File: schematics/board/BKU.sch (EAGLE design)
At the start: 69 parts, among them Q1 8MHz, Q2 32,768KHz, U1 STM32F405RGT6

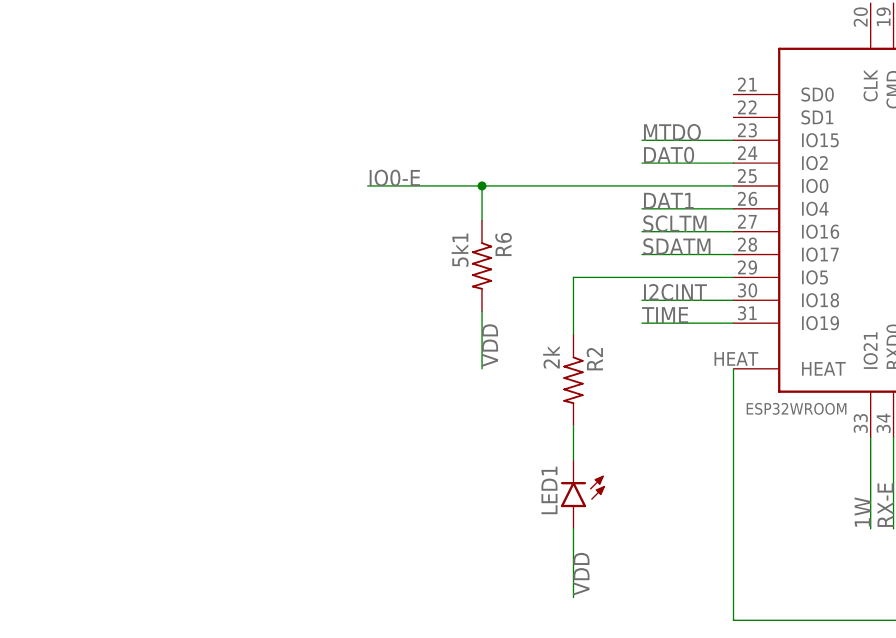
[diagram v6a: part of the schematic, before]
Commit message: Добавлены подтяжки i2c
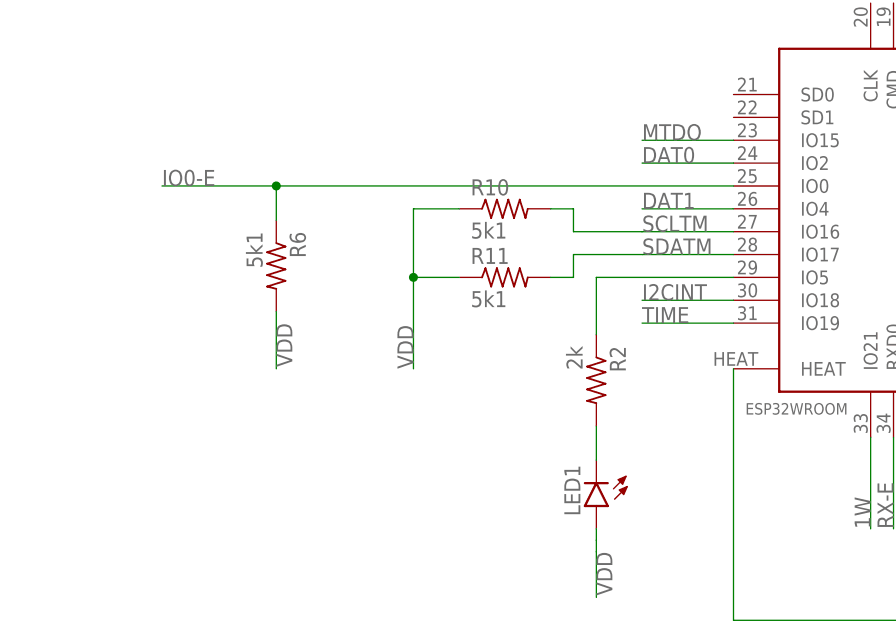
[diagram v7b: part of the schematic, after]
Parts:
- added R10, R11: 5k1, resistor:R-US_R0603
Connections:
- net SCLTM: now also R10.2
- net SDATM: now also R11.2
- net VDD: now also R10.1, R11.1
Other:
- moved on the sheet: LED1, R2, R6
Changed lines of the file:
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@@
 <part name="R4" library="resistor" library_urn="urn:adsk.eagle:library:348" deviceset="R-US_" device="R0603" package3d_urn="urn:adsk.eagle:package:23555/3" value="620R"/>
 <part name="BT1" library="SparkFun-Batteries" deviceset="BATTERY" device="-6.8MM_SMD" value="6.8MM_COIN_CELL"/>
+<part name="R10" library="resistor" library_urn="urn:adsk.eagle:library:348" deviceset="R-US_" device="R0603" package3d_urn="urn:adsk.eagle:package:23555/3" value="5k1"/>
+<part name="R11" library="resistor" library_urn="urn:adsk.eagle:library:348" deviceset="R-US_" device="R0603" package3d_urn="urn:adsk.eagle:package:23555/3" value="5k1"/>
 </parts>
 <sheets>
@@
 <attribute name="VALUE" x="104.902" y="45.72" size="1.778" layer="96" rot="R90"/>
 </instance>
-<instance part="R6" gate="G$1" x="15.24" y="46.99" smashed="yes" rot="R270">
-<attribute name="NAME" x="16.7386" y="50.8" size="1.778" layer="95" rot="R270"/>
-<attribute name="VALUE" x="11.938" y="50.8" size="1.778" layer="96" rot="R270"/>
+<instance part="R6" gate="G$1" x="-7.62" y="46.99" smashed="yes" rot="R270">
+<attribute name="NAME" x="-6.1214" y="50.8" size="1.778" layer="95" rot="R270"/>
+<attribute name="VALUE" x="-10.922" y="50.8" size="1.778" layer="96" rot="R270"/>
 </instance>
 <instance part="U$4" gate="G$1" x="-86.36" y="172.72" smashed="yes"/>
@@
 <instance part="U$19" gate="G$1" x="119.38" y="226.06" smashed="yes"/>
 <instance part="U$20" gate="G$1" x="119.38" y="185.42" smashed="yes"/>
-<instance part="R2" gate="G$1" x="25.4" y="34.29" smashed="yes" rot="R270">
-<attribute name="NAME" x="26.8986" y="38.1" size="1.778" layer="95" rot="R270"/>
-<attribute name="VALUE" x="22.098" y="38.1" size="1.778" layer="96" rot="R270"/>
-</instance>
-<instance part="LED1" gate="G$1" x="25.4" y="20.32" smashed="yes" rot="R180">
-<attribute name="NAME" x="21.844" y="24.892" size="1.778" layer="95" rot="R270"/>
-<attribute name="VALUE" x="19.685" y="24.892" size="1.778" layer="96" rot="R270"/>
+<instance part="R2" gate="G$1" x="27.94" y="34.29" smashed="yes" rot="R270">
+<attribute name="NAME" x="29.4386" y="38.1" size="1.778" layer="95" rot="R270"/>
+<attribute name="VALUE" x="24.638" y="38.1" size="1.778" layer="96" rot="R270"/>
+</instance>
+<instance part="LED1" gate="G$1" x="27.94" y="20.32" smashed="yes" rot="R180">
+<attribute name="NAME" x="24.384" y="24.892" size="1.778" layer="95" rot="R270"/>
+<attribute name="VALUE" x="22.225" y="24.892" size="1.778" layer="96" rot="R270"/>
 </instance>
 <instance part="R7" gate="G$1" x="220.98" y="170.18" smashed="yes" rot="R90">
@@
 <attribute name="NAME" x="272.542" y="220.98" size="1.778" layer="95" font="vector" rot="R90" align="bottom-center"/>
 <attribute name="VALUE" x="281.178" y="220.98" size="1.778" layer="96" font="vector" rot="R90" align="top-center"/>
+</instance>
+<instance part="R10" gate="G$1" x="17.78" y="53.34" smashed="yes">
+<attribute name="NAME" x="13.97" y="54.8386" size="1.778" layer="95"/>
+<attribute name="VALUE" x="13.97" y="50.038" size="1.778" layer="96"/>
+</instance>
+<instance part="R11" gate="G$1" x="17.78" y="45.72" smashed="yes">
+<attribute name="NAME" x="13.97" y="47.2186" size="1.778" layer="95"/>
+<attribute name="VALUE" x="13.97" y="42.418" size="1.778" layer="96"/>
 </instance>
 </instances>
@@
 <segment>
 <pinref part="R6" gate="G$1" pin="2"/>
-<wire x1="15.24" y1="41.91" x2="15.24" y2="35.56" width="0.1524" layer="91"/>
-<label x="15.24" y="40.64" size="1.778" layer="95" rot="R270"/>
+<wire x1="-7.62" y1="41.91" x2="-7.62" y2="35.56" width="0.1524" layer="91"/>
+<label x="-7.62" y="40.64" size="1.778" layer="95" rot="R270"/>
 </segment>
 <segment>
@@
 </segment>
 <segment>
-<wire x1="25.4" y1="16.51" x2="25.4" y2="15.24" width="0.1524" layer="91"/>
-<label x="25.4" y="15.24" size="1.778" layer="95" rot="R270"/>
+<wire x1="27.94" y1="16.51" x2="27.94" y2="15.24" width="0.1524" layer="91"/>
+<label x="27.94" y="15.24" size="1.778" layer="95" rot="R270"/>
 <pinref part="LED1" gate="G$1" pin="A"/>
-<wire x1="25.4" y1="15.24" x2="25.4" y2="10.16" width="0.1524" layer="91"/>
-<wire x1="25.4" y1="16.51" x2="25.4" y2="17.78" width="0.1524" layer="91"/>
+<wire x1="27.94" y1="15.24" x2="27.94" y2="10.16" width="0.1524" layer="91"/>
+<wire x1="27.94" y1="16.51" x2="27.94" y2="17.78" width="0.1524" layer="91"/>
 </segment>
 <segment>
@@
 <wire x1="276.86" y1="198.12" x2="276.86" y2="190.5" width="0.1524" layer="91"/>
 <label x="276.86" y="190.5" size="1.778" layer="95" rot="R90"/>
+</segment>
+<segment>
+<pinref part="R11" gate="G$1" pin="1"/>
+<wire x1="12.7" y1="45.72" x2="7.62" y2="45.72" width="0.1524" layer="91"/>
+<pinref part="R10" gate="G$1" pin="1"/>
+<wire x1="12.7" y1="53.34" x2="7.62" y2="53.34" width="0.1524" layer="91"/>
+<wire x1="7.62" y1="53.34" x2="7.62" y2="45.72" width="0.1524" layer="91"/>
+<wire x1="7.62" y1="45.72" x2="7.62" y2="35.56" width="0.1524" layer="91"/>
+<junction x="7.62" y="45.72"/>
+<label x="7.62" y="35.56" size="1.778" layer="95" rot="R90"/>
 </segment>
 </net>
@@
 </segment>
 <segment>
-<label x="2.54" y="55.88" size="1.778" layer="95"/>
-<wire x1="15.24" y1="55.88" x2="43.18" y2="55.88" width="0.1524" layer="91"/>
-<wire x1="2.54" y1="55.88" x2="15.24" y2="55.88" width="0.1524" layer="91"/>
+<label x="-20.32" y="55.88" size="1.778" layer="95"/>
+<wire x1="-7.62" y1="55.88" x2="43.18" y2="55.88" width="0.1524" layer="91"/>
+<wire x1="-20.32" y1="55.88" x2="-7.62" y2="55.88" width="0.1524" layer="91"/>
 <pinref part="R6" gate="G$1" pin="1"/>
-<wire x1="15.24" y1="52.07" x2="15.24" y2="55.88" width="0.1524" layer="91"/>
-<junction x="15.24" y="55.88"/>
+<wire x1="-7.62" y1="52.07" x2="-7.62" y2="55.88" width="0.1524" layer="91"/>
+<junction x="-7.62" y="55.88"/>
 <pinref part="U$13" gate="G$1" pin="IO0"/>
 </segment>
@@
 <label x="33.02" y="50.8" size="1.778" layer="95"/>
 <pinref part="U$13" gate="G$1" pin="IO16"/>
+<wire x1="33.02" y1="50.8" x2="25.4" y2="50.8" width="0.1524" layer="91"/>
+<pinref part="R10" gate="G$1" pin="2"/>
+<wire x1="22.86" y1="53.34" x2="25.4" y2="53.34" width="0.1524" layer="91"/>
+<wire x1="25.4" y1="53.34" x2="25.4" y2="50.8" width="0.1524" layer="91"/>
 </segment>
 </net>
@@
 <label x="33.02" y="48.26" size="1.778" layer="95"/>
 <pinref part="U$13" gate="G$1" pin="IO17"/>
+<wire x1="33.02" y1="48.26" x2="25.4" y2="48.26" width="0.1524" layer="91"/>
+<pinref part="R11" gate="G$1" pin="2"/>
+<wire x1="22.86" y1="45.72" x2="25.4" y2="45.72" width="0.1524" layer="91"/>
+<wire x1="25.4" y1="45.72" x2="25.4" y2="48.26" width="0.1524" layer="91"/>
 </segment>
 </net>
@@
 <segment>
 <pinref part="R2" gate="G$1" pin="1"/>
-<wire x1="25.4" y1="39.37" x2="25.4" y2="45.72" width="0.1524" layer="91"/>
-<wire x1="25.4" y1="45.72" x2="43.18" y2="45.72" width="0.1524" layer="91"/>
+<wire x1="27.94" y1="39.37" x2="27.94" y2="45.72" width="0.1524" layer="91"/>
+<wire x1="27.94" y1="45.72" x2="43.18" y2="45.72" width="0.1524" layer="91"/>
 <pinref part="U$13" gate="G$1" pin="IO5"/>
 </segment>
@@
 <segment>
 <pinref part="LED1" gate="G$1" pin="C"/>
-<wire x1="25.4" y1="25.4" x2="25.4" y2="29.21" width="0.1524" layer="91"/>
+<wire x1="27.94" y1="25.4" x2="27.94" y2="29.21" width="0.1524" layer="91"/>
 <pinref part="R2" gate="G$1" pin="2"/>
 </segment>

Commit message: Добавлены новые диоды
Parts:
- added JP1: (no value), pinheadCS:PINHD-1X2
- added R14: 10k, resistor:R-US_R0603
- C14: device rcl:C-USC1206 -> rcl:C-USC0603
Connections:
- new net N$5: JP1.2, R14.1, U1.PB9
- net 5V: now also GPS.UCC
- net GND: now also R14.2
- net VDD: now also JP1.1; no longer GPS.UCC
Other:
- moved on the sheet: LED2, R15
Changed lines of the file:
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@@
 <part name="R12" library="resistor" library_urn="urn:adsk.eagle:library:348" deviceset="R-US_" device="R0603" package3d_urn="urn:adsk.eagle:package:23555/3" value="73,2k"/>
 <part name="R13" library="resistor" library_urn="urn:adsk.eagle:library:348" deviceset="R-US_" device="R0603" package3d_urn="urn:adsk.eagle:package:23555/3" value="45,3k"/>
-<part name="C14" library="rcl" library_urn="urn:adsk.eagle:library:334" deviceset="C-US" device="C1206" package3d_urn="urn:adsk.eagle:package:23618/2" value="2,2µ"/>
+<part name="C14" library="rcl" library_urn="urn:adsk.eagle:library:334" deviceset="C-US" device="C0603" package3d_urn="urn:adsk.eagle:package:23616/2" value="2,2µ"/>
 <part name="C6" library="rcl" library_urn="urn:adsk.eagle:library:334" deviceset="C-US" device="C1206" package3d_urn="urn:adsk.eagle:package:23618/2" value="22µ"/>
 <part name="C15" library="rcl" library_urn="urn:adsk.eagle:library:334" deviceset="C-US" device="C1206" package3d_urn="urn:adsk.eagle:package:23618/2" value="22µ"/>
@@
 <part name="R10" library="resistor" library_urn="urn:adsk.eagle:library:348" deviceset="R-US_" device="R0603" package3d_urn="urn:adsk.eagle:package:23555/3" value="5k1"/>
 <part name="R11" library="resistor" library_urn="urn:adsk.eagle:library:348" deviceset="R-US_" device="R0603" package3d_urn="urn:adsk.eagle:package:23555/3" value="5k1"/>
+<part name="JP1" library="pinheadCS" deviceset="PINHD-1X2" device=""/>
+<part name="R14" library="resistor" library_urn="urn:adsk.eagle:library:348" deviceset="R-US_" device="R0603" package3d_urn="urn:adsk.eagle:package:23555/3" value="10k"/>
 </parts>
 <sheets>
@@
 <attribute name="VALUE" x="-78.74" y="57.15" size="1.778" layer="96" rot="R90"/>
 </instance>
-<instance part="R15" gate="G$1" x="309.88" y="149.86" smashed="yes" rot="R90">
-<attribute name="NAME" x="308.3814" y="146.05" size="1.778" layer="95" rot="R90"/>
-<attribute name="VALUE" x="313.182" y="146.05" size="1.778" layer="96" rot="R90"/>
+<instance part="R15" gate="G$1" x="320.04" y="149.86" smashed="yes" rot="R90">
+<attribute name="NAME" x="318.5414" y="146.05" size="1.778" layer="95" rot="R90"/>
+<attribute name="VALUE" x="323.342" y="146.05" size="1.778" layer="96" rot="R90"/>
 </instance>
 <instance part="R17" gate="G$1" x="302.26" y="86.36" smashed="yes" rot="R90">
@@
 <attribute name="VALUE" x="75.184" y="227.711" size="1.778" layer="96" rot="R180"/>
 </instance>
-<instance part="LED2" gate="G$1" x="309.88" y="162.56" smashed="yes">
-<attribute name="NAME" x="313.436" y="157.988" size="1.778" layer="95" rot="R90"/>
-<attribute name="VALUE" x="315.595" y="157.988" size="1.778" layer="96" rot="R90"/>
+<instance part="LED2" gate="G$1" x="320.04" y="162.56" smashed="yes">
+<attribute name="NAME" x="323.596" y="157.988" size="1.778" layer="95" rot="R90"/>
+<attribute name="VALUE" x="325.755" y="157.988" size="1.778" layer="96" rot="R90"/>
 </instance>
 <instance part="LED3" gate="G$1" x="177.8" y="91.44" smashed="yes" rot="R270">
@@
 <attribute name="VALUE" x="13.97" y="42.418" size="1.778" layer="96"/>
 </instance>
+<instance part="JP1" gate="G$1" x="208.28" y="119.38" smashed="yes" rot="R90">
+<attribute name="NAME" x="202.565" y="113.03" size="1.778" layer="95" rot="R90"/>
+<attribute name="VALUE" x="213.36" y="113.03" size="1.778" layer="96" rot="R90"/>
+</instance>
+<instance part="R14" gate="G$1" x="203.2" y="106.68" smashed="yes" rot="R180">
+<attribute name="NAME" x="207.01" y="105.1814" size="1.778" layer="95" rot="R180"/>
+<attribute name="VALUE" x="207.01" y="109.982" size="1.778" layer="96" rot="R180"/>
+</instance>
 </instances>
 <busses>
@@
 <label x="276.86" y="228.6" size="1.778" layer="95" rot="R90"/>
 </segment>
+<segment>
+<pinref part="R14" gate="G$1" pin="2"/>
+<wire x1="198.12" y1="106.68" x2="190.5" y2="106.68" width="0.1524" layer="91"/>
+<label x="195.58" y="106.68" size="1.778" layer="95" rot="R180"/>
+</segment>
 </net>
 <net name="5V" class="0">
@@
 <label x="220.98" y="266.7" size="1.778" layer="95" rot="R90"/>
 </segment>
+<segment>
+<pinref part="GPS" gate="G$1" pin="UCC"/>
+<wire x1="246.38" y1="198.12" x2="246.38" y2="193.04" width="0.1524" layer="91"/>
+<wire x1="246.38" y1="193.04" x2="254" y2="193.04" width="0.1524" layer="91"/>
+<label x="248.92" y="193.04" size="1.778" layer="95"/>
+</segment>
 </net>
 <net name="1W" class="0">
@@
 </segment>
 <segment>
-<pinref part="GPS" gate="G$1" pin="UCC"/>
-<wire x1="246.38" y1="198.12" x2="246.38" y2="193.04" width="0.1524" layer="91"/>
-<wire x1="246.38" y1="193.04" x2="254" y2="193.04" width="0.1524" layer="91"/>
-<label x="248.92" y="193.04" size="1.778" layer="95"/>
-</segment>
-<segment>
 <pinref part="LED2" gate="G$1" pin="A"/>
 <pinref part="U1" gate="G$1" pin="VDD"/>
@@
 <label x="297.18" y="165.1" size="1.778" layer="95"/>
 <junction x="292.1" y="172.72"/>
-<wire x1="309.88" y1="165.1" x2="292.1" y2="165.1" width="0.1524" layer="91"/>
+<wire x1="320.04" y1="165.1" x2="292.1" y2="165.1" width="0.1524" layer="91"/>
 <wire x1="292.1" y1="165.1" x2="292.1" y2="172.72" width="0.1524" layer="91"/>
 </segment>
@@
 <label x="7.62" y="35.56" size="1.778" layer="95" rot="R90"/>
 </segment>
+<segment>
+<pinref part="JP1" gate="G$1" pin="1"/>
+<wire x1="205.74" y1="116.84" x2="190.5" y2="116.84" width="0.1524" layer="91"/>
+<label x="195.58" y="116.84" size="1.778" layer="95" rot="R180"/>
+</segment>
 </net>
 <net name="N$24" class="0">
@@
 <segment>
 <pinref part="U1" gate="G$1" pin="PC12"/>
-<wire x1="292.1" y1="129.54" x2="309.88" y2="129.54" width="0.1524" layer="91"/>
-<wire x1="309.88" y1="129.54" x2="309.88" y2="144.78" width="0.1524" layer="91"/>
+<wire x1="292.1" y1="129.54" x2="320.04" y2="129.54" width="0.1524" layer="91"/>
+<wire x1="320.04" y1="129.54" x2="320.04" y2="144.78" width="0.1524" layer="91"/>
 <pinref part="R15" gate="G$1" pin="1"/>
 </segment>
@@
 <pinref part="R15" gate="G$1" pin="2"/>
 <pinref part="LED2" gate="G$1" pin="C"/>
-<wire x1="309.88" y1="157.48" x2="309.88" y2="154.94" width="0.1524" layer="91"/>
+<wire x1="320.04" y1="157.48" x2="320.04" y2="154.94" width="0.1524" layer="91"/>
 </segment>
 </net>
@@
 </segment>
 </net>
+<net name="N$5" class="0">
+<segment>
+<pinref part="JP1" gate="G$1" pin="2"/>
+<wire x1="208.28" y1="99.06" x2="208.28" y2="106.68" width="0.1524" layer="91"/>
+<pinref part="R14" gate="G$1" pin="1"/>
+<wire x1="208.28" y1="106.68" x2="208.28" y2="116.84" width="0.1524" layer="91"/>
+<junction x="208.28" y="106.68"/>
+<wire x1="208.28" y1="99.06" x2="228.6" y2="99.06" width="0.1524" layer="91"/>
+<wire x1="228.6" y1="99.06" x2="228.6" y2="93.98" width="0.1524" layer="91"/>
+<pinref part="U1" gate="G$1" pin="PB9"/>
+<wire x1="228.6" y1="93.98" x2="231.14" y2="93.98" width="0.1524" layer="91"/>
+</segment>
+</net>
